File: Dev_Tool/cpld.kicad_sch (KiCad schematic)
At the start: 17 parts, among them J6 JTAG, U10 EPM7032SLC44-10, U12 SN74LVC1G07DBV, U13 SN74LVC1G07DBV, U14 SN74LVC1G07DBV, U15 SN74LVC1G07DBV, U16 SN74LVC1G07DBV, U17 SN74LVC1G07DBV, U18 SN74LVC1G07DBV, U19 SN74LVC1G07DBV, U20 SN74LVC1G07DBV

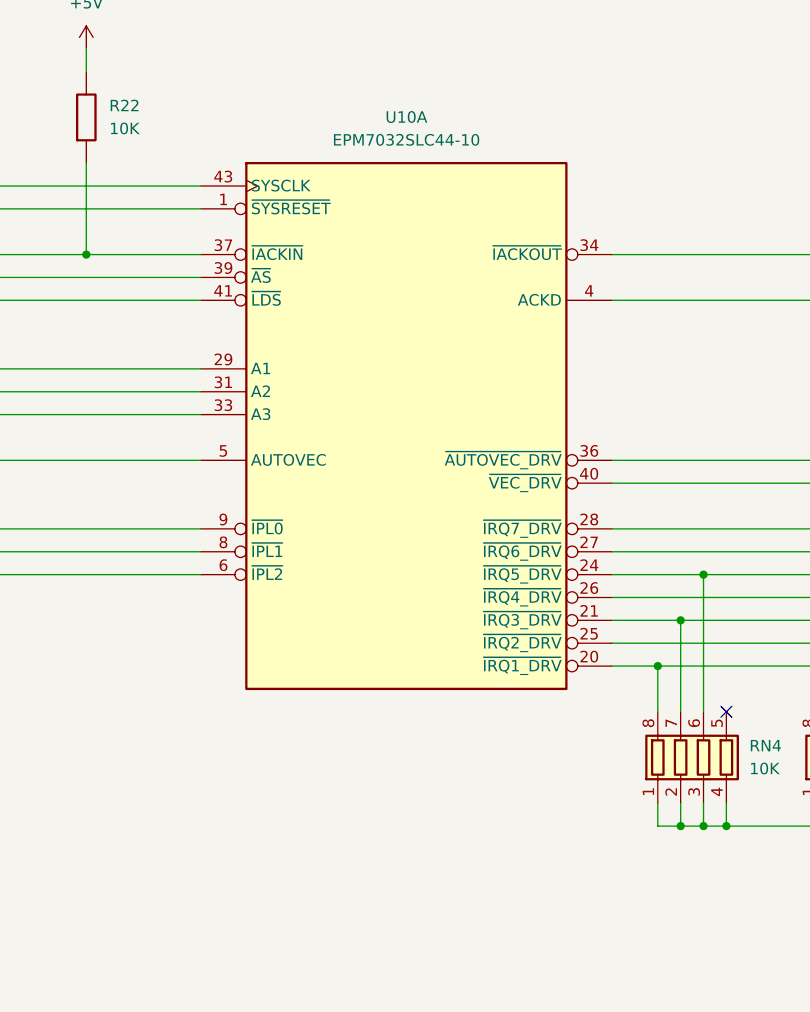
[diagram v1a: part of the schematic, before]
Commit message: Add unconnected pins to CPLD symbol
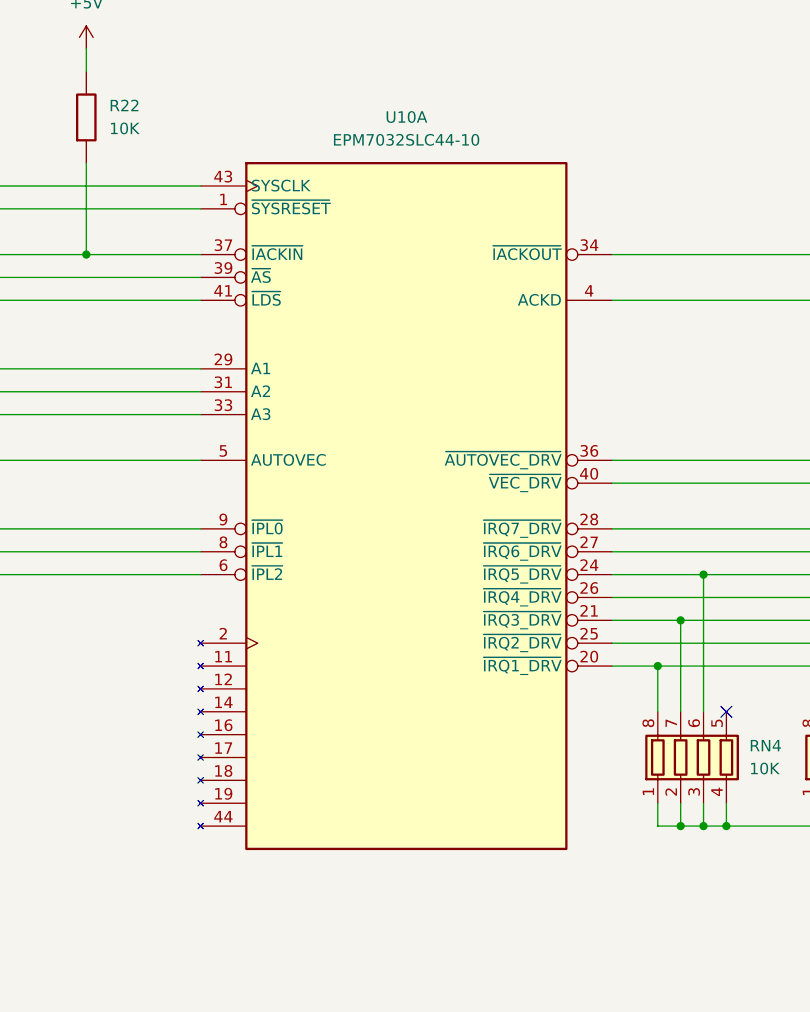
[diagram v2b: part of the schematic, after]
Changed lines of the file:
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@@
 	(title_block
 		(title "INTERRUPT CPLD")
-		(date "2025-09-08")
+		(date "2025-09-09")
 		(rev "1")
 		(company "(C) TOM STOREY")
@@
 	(symbol
 		(lib_id "Dev_Tool:EPM7032SLC44-10")
-		(at 99.06 63.5 0)
+		(at 99.06 71.12 0)
 		(unit 1)
 		(exclude_from_sim no)
@@
 		(on_board yes)
 		(dnp no)
-		(fields_autoplaced yes)
 		(property "Reference" "U10"
 			(at 99.06 30.48 0)
@@
 		)
 		(property "Footprint" "COMET_footprints:Package_PLCC-44_SMD_Socket"
-			(at 99.06 63.5 0)
+			(at 99.06 71.12 0)
 			(effects
 				(font
@@
 		)
 		(property "Datasheet" ""
-			(at 99.06 63.5 0)
+			(at 99.06 71.12 0)
 			(effects
 				(font
@@
 		)
 		(property "Description" ""
-			(at 99.06 63.5 0)
+			(at 99.06 71.12 0)
 			(effects
 				(font
@@
 		(pin "42"
 		)
+		(pin "12"
+		)
+		(pin "2"
+		)
+		(pin "11"
+		)
+		(pin "17"
+		)
+		(pin "19"
+		)
+		(pin "14"
+		)
+		(pin "16"
+		)
+		(pin "44"
+		)
+		(pin "18"
+		)
 		(instances
 			(project ""
@@
 		(pin "42"
 		)
+		(pin "17"
+		)
+		(pin "19"
+		)
+		(pin "44"
+		)
+		(pin "2"
+		)
+		(pin "16"
+		)
+		(pin "18"
+		)
+		(pin "12"
+		)
+		(pin "11"
+		)
+		(pin "14"
+		)
 		(instances
